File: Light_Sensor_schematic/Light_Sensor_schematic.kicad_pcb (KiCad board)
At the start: 2 copper layers, 50 x 50 mm, 21 parts, among them IC1 TSL237S-LF, J1 Conn_01x03, J3 Conn_01x04_Male, U1 STM32L432KCUx, U2 STDC14, U3 TG-3541CE

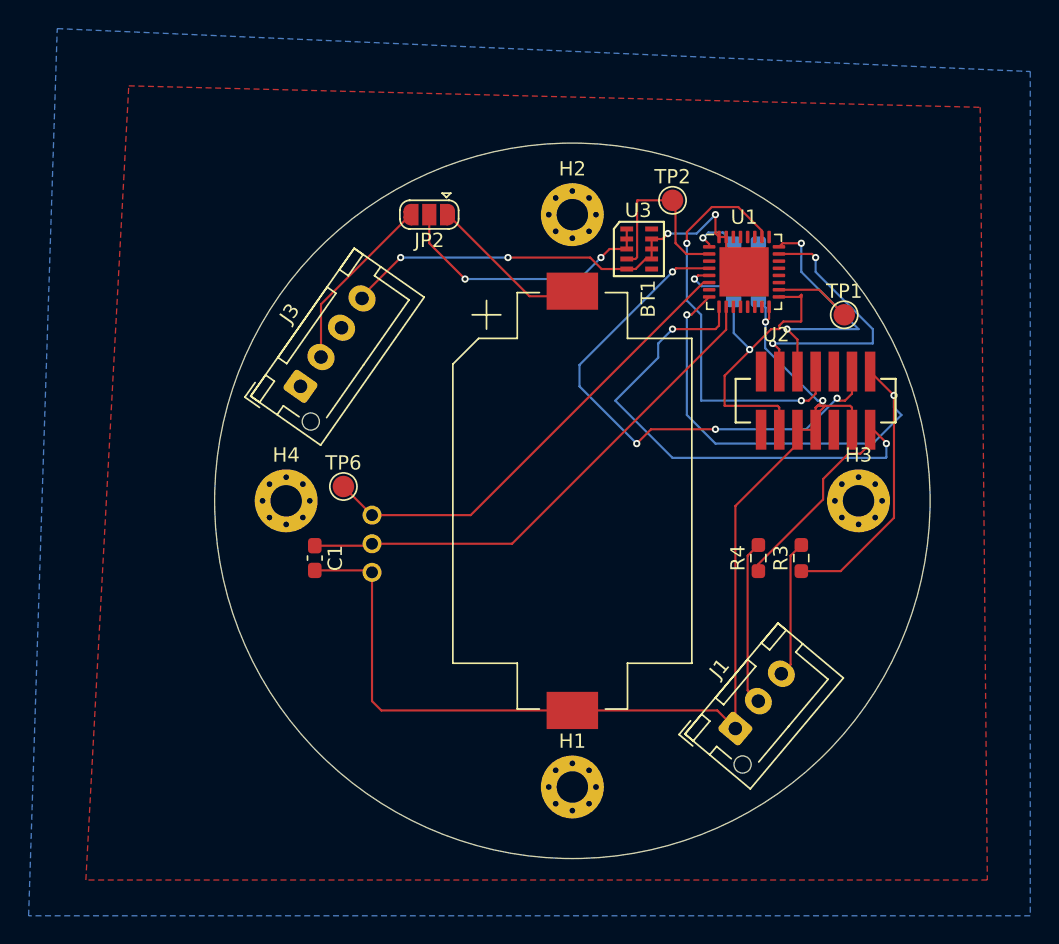
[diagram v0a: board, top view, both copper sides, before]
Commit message: Kicad5 to 6
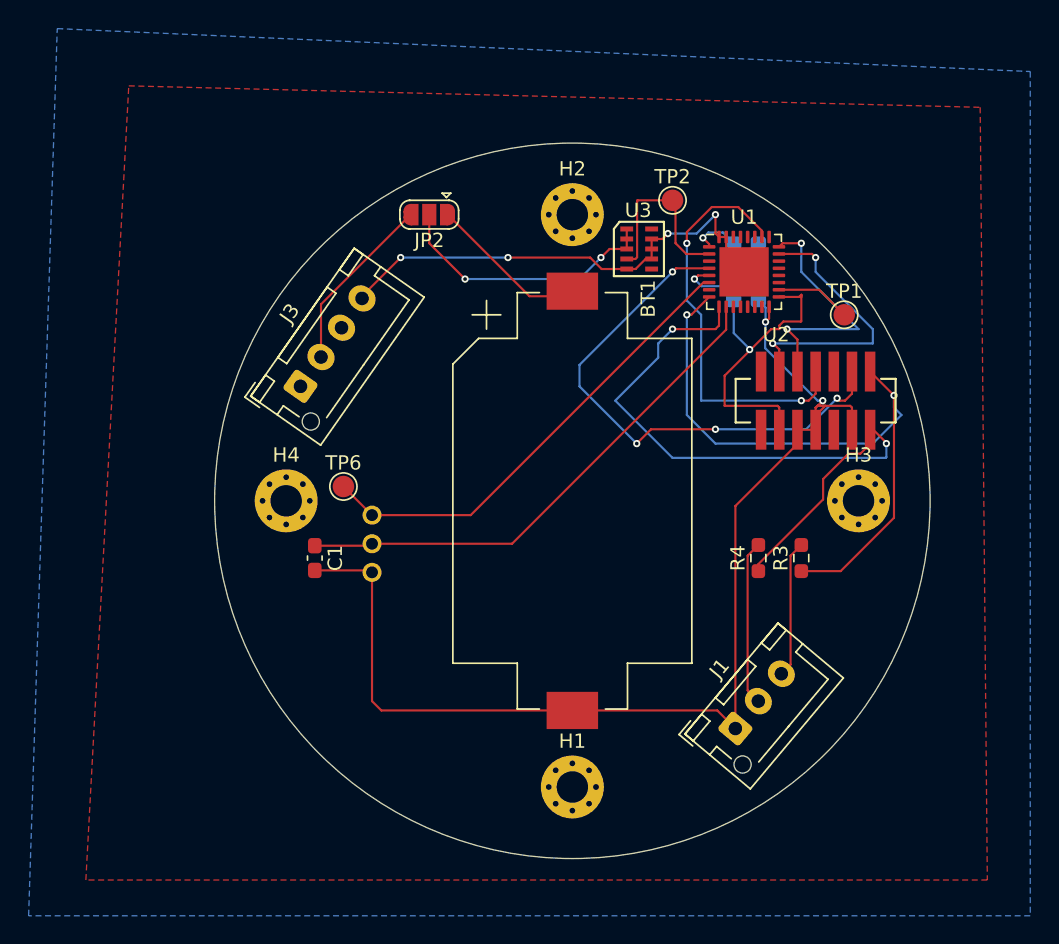
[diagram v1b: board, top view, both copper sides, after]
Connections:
- J3 pad 1: Net-(J3-Pad1) -> unconnected-(J3-Pad1)
- J3 pad 3: Net-(J3-Pad3) -> unconnected-(J3-Pad3)
- U1 pad 11: Net-(U1-Pad11) -> unconnected-(U1-Pad11)
- U1 pad 12: Net-(U1-Pad12) -> unconnected-(U1-Pad12)
- U1 pad 13: Net-(U1-Pad13) -> unconnected-(U1-Pad13)
- U1 pad 14: Net-(U1-Pad14) -> unconnected-(U1-Pad14)
- U1 pad 15: Net-(U1-Pad15) -> unconnected-(U1-Pad15)
- U1 pad 19: Net-(U1-Pad19) -> unconnected-(U1-Pad19)
- U1 pad 20: Net-(U1-Pad20) -> unconnected-(U1-Pad20)
- U1 pad 21: Net-(U1-Pad21) -> unconnected-(U1-Pad21)
- U1 pad 22: Net-(U1-Pad22) -> unconnected-(U1-Pad22)
- U1 pad 25: Net-(U1-Pad25) -> unconnected-(U1-Pad25)
- U1 pad 27: Net-(U1-Pad27) -> unconnected-(U1-Pad27)
- U1 pad 28: Net-(U1-Pad28) -> unconnected-(U1-Pad28)
- U1 pad 29: Net-(U1-Pad29) -> unconnected-(U1-Pad29)
- U1 pad 3: Net-(U1-Pad3) -> unconnected-(U1-Pad3)
- U1 pad 30: Net-(U1-Pad30) -> unconnected-(U1-Pad30)
- U1 pad 7: Net-(U1-Pad7) -> unconnected-(U1-Pad7)
- U2 pad 1: Net-(U2-Pad1) -> unconnected-(U2-Pad1)
- U2 pad 10: Net-(U2-Pad10) -> unconnected-(U2-Pad10)
- U2 pad 2: Net-(U2-Pad2) -> unconnected-(U2-Pad2)
- U2 pad 9: Net-(U2-Pad9) -> unconnected-(U2-Pad9)
- U3 pad 10: Net-(U3-Pad10) -> unconnected-(U3-Pad10)
- U3 pad 6: Net-(U3-Pad6) -> unconnected-(U3-Pad6)
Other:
- net class Default removed
- rule pad_to_mask_clearance: 0 -> 0.0508

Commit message: corrected DRC errors to allow import at macrofab.
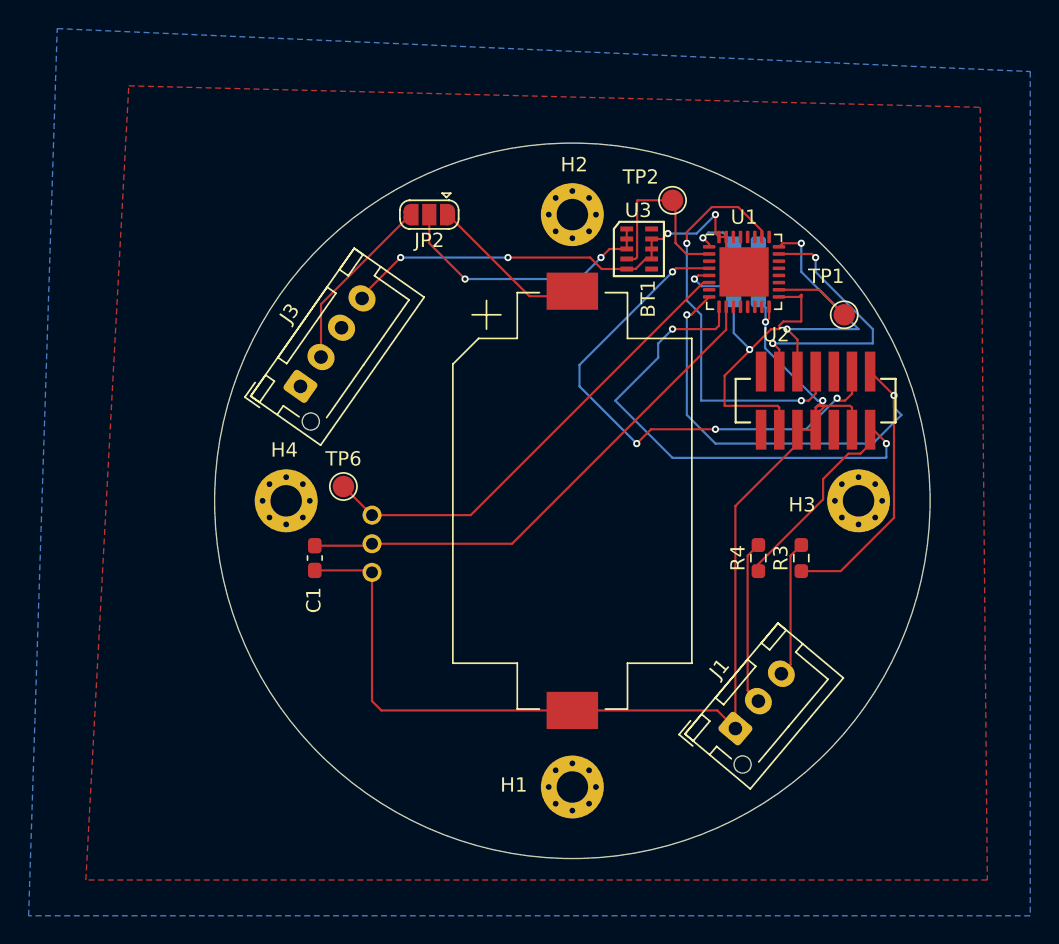
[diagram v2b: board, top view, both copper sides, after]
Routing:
- net /SWDCLK: track 18.8 -> 17.6 mm
- net Net-(BT1-Pad1): track 12.1 -> 11.4 mm
- net VDD: track 50.2 -> 49.7 mm
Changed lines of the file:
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@@
     (property "Sheetname" "")
     (attr smd)
-    (fp_text reference "C1" (at 0 -1.43 90) (layer "F.SilkS")
+    (fp_text reference "C1" (at 2.94 0.07 90) (layer "F.SilkS")
       (effects (font (size 1 1) (thickness 0.15)))
     )
@@
     (property "Sheetname" "")
     (attr exclude_from_pos_files)
-    (fp_text reference "H1" (at 0 -3.2) (layer "F.SilkS")
+    (fp_text reference "H1" (at -4.09 -0.14) (layer "F.SilkS")
       (effects (font (size 1 1) (thickness 0.15)))
     )
@@
     (property "Sheetname" "")
     (attr exclude_from_pos_files)
-    (fp_text reference "H2" (at 0 -3.2) (layer "F.SilkS")
+    (fp_text reference "H2" (at 0.13 -3.49) (layer "F.SilkS")
       (effects (font (size 1 1) (thickness 0.15)))
     )
@@
     (property "Sheetname" "")
     (attr exclude_from_pos_files)
-    (fp_text reference "H3" (at 0 -3.2) (layer "F.SilkS")
+    (fp_text reference "H3" (at -3.95 0.28) (layer "F.SilkS")
       (effects (font (size 1 1) (thickness 0.15)))
     )
@@
     (property "Sheetname" "")
     (attr exclude_from_pos_files)
-    (fp_text reference "H4" (at 0 -3.2) (layer "F.SilkS")
+    (fp_text reference "H4" (at -0.13 -3.55) (layer "F.SilkS")
       (effects (font (size 1 1) (thickness 0.15)))
     )
@@
     (property "Sheetname" "")
     (attr exclude_from_pos_files)
-    (fp_text reference "TP1" (at 0 -1.648) (layer "F.SilkS")
+    (fp_text reference "TP1" (at -1.26 -2.69) (layer "F.SilkS")
       (effects (font (size 1 1) (thickness 0.15)))
     )
@@
     (property "Sheetname" "")
     (attr exclude_from_pos_files)
-    (fp_text reference "TP2" (at 0 -1.648) (layer "F.SilkS")
+    (fp_text reference "TP2" (at -2.22 -1.63) (layer "F.SilkS")
       (effects (font (size 1 1) (thickness 0.15)))
     )
@@
     (property "Sheetname" "")
     (attr exclude_from_pos_files)
-    (fp_text reference "TP6" (at 0 -1.648) (layer "F.SilkS")
+    (fp_text reference "TP6" (at 0.01 -1.93) (layer "F.SilkS")
       (effects (font (size 1 1) (thickness 0.15)))
     )
@@
     (property "Sheetname" "")
     (attr smd)
-    (fp_text reference "C2" (at 0 1.43) (layer "B.SilkS")
+    (fp_text reference "C2" (at 2.5625 -0.132) (layer "B.SilkS")
       (effects (font (size 1 1) (thickness 0.15)) (justify mirror))
     )
@@
     (property "Sheetname" "")
     (attr smd)
-    (fp_text reference "C4" (at 0 1.43) (layer "B.SilkS")
+    (fp_text reference "C4" (at 2.5625 -0.1) (layer "B.SilkS")
       (effects (font (size 1 1) (thickness 0.15)) (justify mirror))
     )
@@
     (property "Sheetname" "")
     (attr smd)
-    (fp_text reference "C6" (at 0 1.43) (layer "B.SilkS")
+    (fp_text reference "C6" (at 0.0425 1.57) (layer "B.SilkS")
       (effects (font (size 1 1) (thickness 0.15)) (justify mirror))
     )
@@
     (property "Sheetname" "")
     (attr through_hole)
-    (fp_text reference "IC1" (at -0.151 1.731 90) (layer "B.SilkS")
+    (fp_text reference "IC1" (at 4.66 0.72 90) (layer "B.SilkS")
       (effects (font (size 1.27 1.27) (thickness 0.254)) (justify mirror))
     )
-    (fp_text value "TSL237S-LF" (at -0.151 1.731 90) (layer "B.SilkS") hide
+    (fp_text value "TSL237S-LF" (at -0.32 3.59 90) (layer "B.SilkS") hide
       (effects (font (size 1.27 1.27) (thickness 0.254)) (justify mirror))
     )
@@
   (segment (start 140.73 101.024162) (end 140.73 100.032) (width 0.1524) (layer "F.Cu") (net 1))
   (segment (start 142 98.4846) (end 142.0154 98.4846) (width 0.1524) (layer "F.Cu") (net 1))
-  (segment (start 138.75 91.85401) (end 138.75 91.4375) (width 0.1524) (layer "F.Cu") (net 1))
   (segment (start 138.75 92.25) (end 138.75 91.4375) (width 0.1524) (layer "F.Cu") (net 1))
   (segment (start 144.54 100.032) (end 144.54 98.4846) (width 0.1524) (layer "F.Cu") (net 1))
@@
   (segment (start 122.002409 90.702409) (end 125.145973 90.702409) (width 0.1524) (layer "F.Cu") (net 2))
   (segment (start 125.145973 90.702409) (end 125.249191 90.599191) (width 0.1524) (layer "F.Cu") (net 2))
-  (segment (start 125.55 89.8) (end 125 90.35) (width 0.1524) (layer "F.Cu") (net 2))
   (segment (start 116.3 85) (end 122.002409 90.702409) (width 0.1524) (layer "F.Cu") (net 2))
   (segment (start 133.7802 89.25) (end 133.5302 89.5) (width 0.1524) (layer "F.Cu") (net 3))
@@
   (segment (start 141 90.60241) (end 141 90.7802) (width 0.1524) (layer "F.Cu") (net 3))
   (segment (start 127.6 87.4) (end 128.8 87.4) (width 0.1524) (layer "F.Cu") (net 3))
-  (segment (start 134.5625 87.25) (end 134.25 87.25) (width 0.1524) (layer "F.Cu") (net 3))
   (segment (start 135.639201 96.256637) (end 138.895838 93) (width 0.1524) (layer "F.Cu") (net 3))
   (segment (start 139.469799 92.745503) (end 139.745503 92.469799) (width 0.1524) (layer "F.Cu") (net 3))
@@
   (segment (start 136.275 93.275) (end 137.428336 94.428336) (width 0.1524) (layer "B.Cu") (net 3))
   (segment (start 117.5 89.5) (end 125.5 89.5) (width 0.1524) (layer "B.Cu") (net 3))
-  (segment (start 136 89) (end 136.275 89) (width 0.1524) (layer "B.Cu") (net 3))
   (segment (start 134.0302 90) (end 136 90) (width 0.1524) (layer "B.Cu") (net 3))
   (segment (start 136 89.275) (end 136.275 89) (width 0.1524) (layer "B.Cu") (net 3))
@@
   (segment (start 140.73 93.73) (end 140 93) (width 0.1524) (layer "F.Cu") (net 28))
   (segment (start 141 87) (end 139.6875 87) (width 0.1524) (layer "F.Cu") (net 28))
-  (segment (start 140.73 95.968) (end 140.73 94.73) (width 0.1524) (layer "F.Cu") (net 28))
   (segment (start 140.73 95.968) (end 140.73 93.73) (width 0.1524) (layer "F.Cu") (net 28))
   (via (at 140 93) (size 0.508) (drill 0.254) (layers "F.Cu" "B.Cu") (net 28))
